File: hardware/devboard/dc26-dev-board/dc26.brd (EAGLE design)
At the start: 126 x 70 mm, 104 parts, among them CN1 JST, IC3 LDL112D33R, J1 DC26 Shitty AddOn, J2 DC26 Shitty AddOn, P1 SSSS811101, Y1 ABL-8.000MHZ-B2

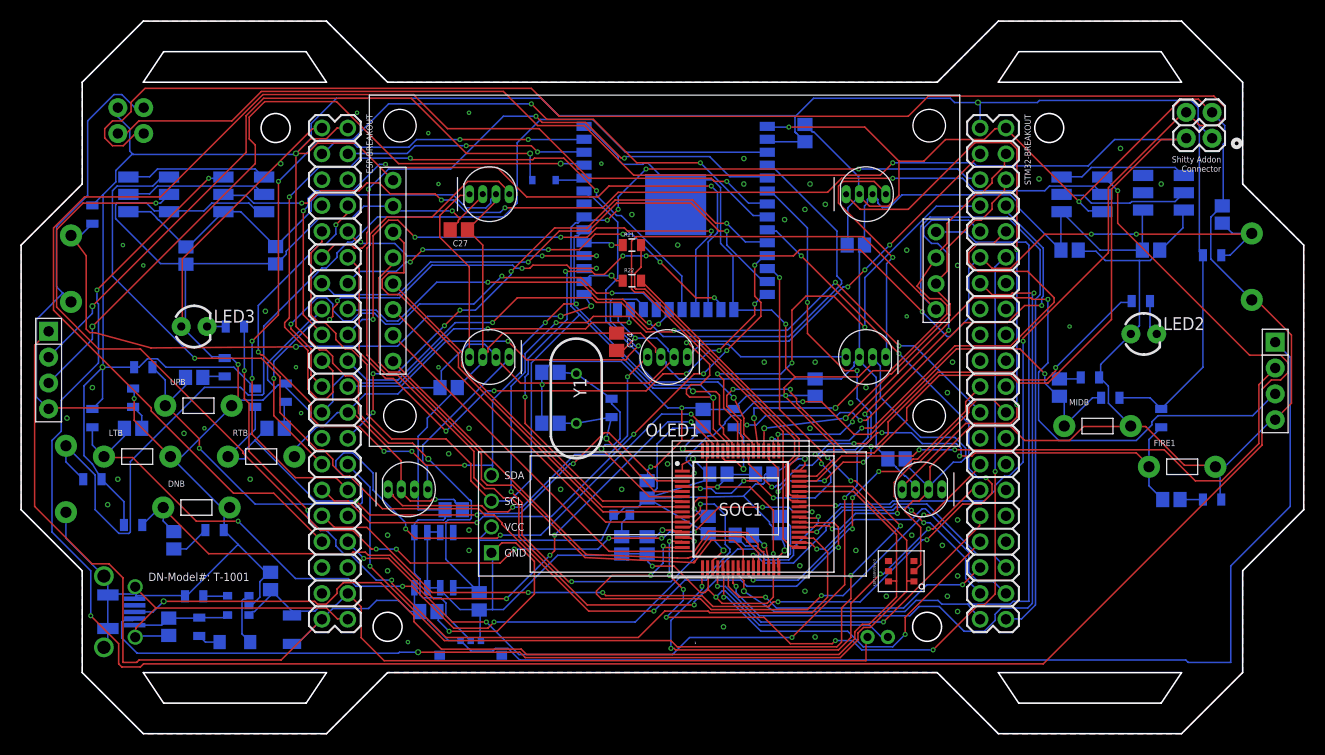
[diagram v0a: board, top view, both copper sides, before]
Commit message: logo causing 0 width polys will fix later
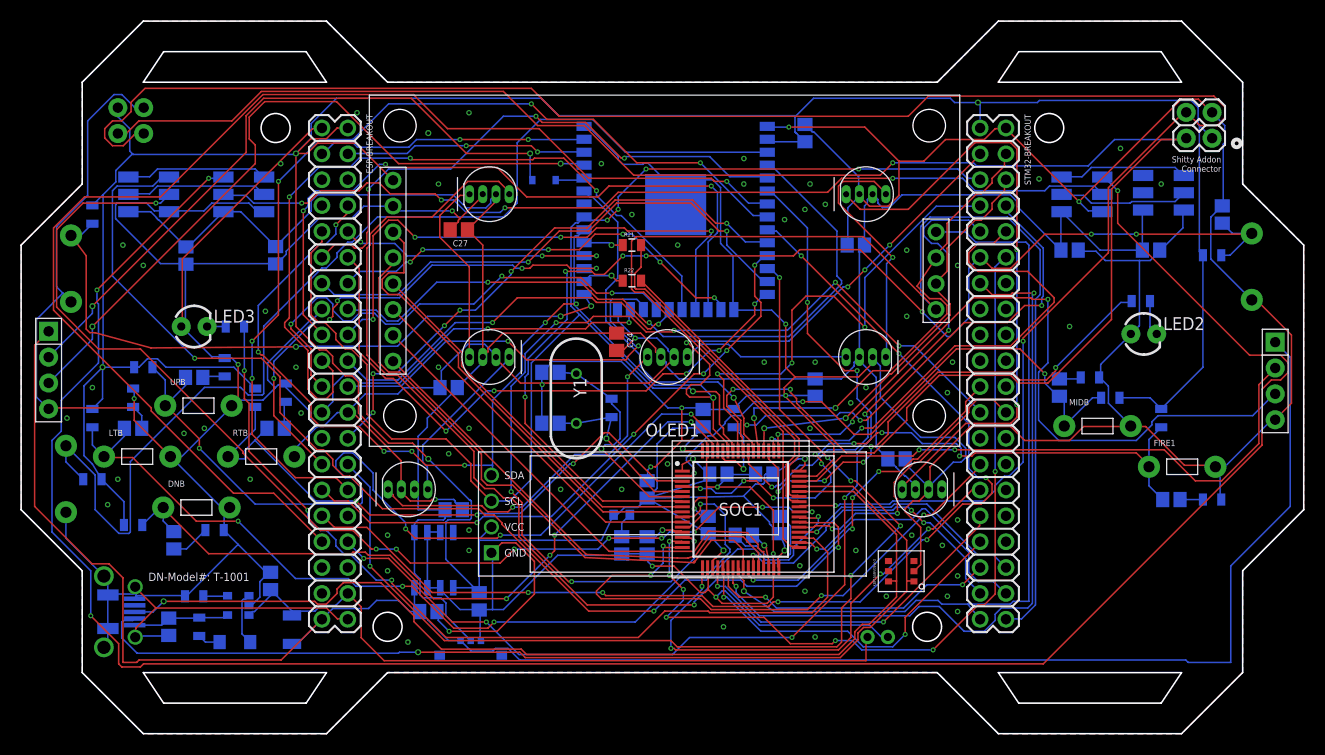
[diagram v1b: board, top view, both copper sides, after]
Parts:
- removed U$1: KRUX_LOGO, dc-26:KRUX_LOGO
- removed U$2: CMD_C0DE_LOGO, dc-26:CMD_C0DE_LOGO
- removed U$3: DARKNET_DD, dc-26:DARKNET_D
- removed U$4: DARKNET_NN, dc-26:DARKNET_N
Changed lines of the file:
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@@
 <setting verticaltext="up"/>
 </settings>
-<grid distance="1" unitdist="mm" unit="mm" style="lines" multiple="1" display="yes" altdistance="0.5" altunitdist="mm" altunit="mm"/>
+<grid distance="39.3700787" unitdist="mil" unit="mil" style="lines" multiple="1" display="yes" altdistance="19.6850394" altunitdist="mil" altunit="mil"/>
 <layers>
 <layer number="1" name="Top" color="4" fill="1" visible="yes" active="yes"/>
@@
 <layer number="27" name="tValues" color="7" fill="1" visible="yes" active="yes"/>
 <layer number="28" name="bValues" color="7" fill="1" visible="yes" active="yes"/>
-<layer number="29" name="tStop" color="7" fill="3" visible="yes" active="yes"/>
+<layer number="29" name="tStop" color="7" fill="3" visible="no" active="yes"/>
 <layer number="30" name="bStop" color="7" fill="6" visible="no" active="yes"/>
 <layer number="31" name="tCream" color="7" fill="4" visible="no" active="yes"/>
@@
 <layer number="119" name="mUnrouted" color="7" fill="1" visible="no" active="yes"/>
 <layer number="120" name="mDimension" color="7" fill="1" visible="no" active="yes"/>
-<layer number="121" name="_tsilk" color="7" fill="1" visible="yes" active="yes"/>
+<layer number="121" name="_tsilk" color="7" fill="1" visible="no" active="yes"/>
 <layer number="122" name="_bsilk" color="7" fill="1" visible="no" active="yes"/>
 <layer number="123" name="tTestmark" color="7" fill="1" visible="no" active="yes"/>
@@
 <circle x="91" y="10.5" radius="1.425" width="0.1524" layer="20"/>
 <circle x="103" y="59.5" radius="1.425" width="0.1524" layer="20"/>
-<text x="104" y="11" size="1.4224" layer="29" font="vector">Darknet
+<text x="104" y="11" size="1.4224" layer="29">Darknet
 Indusries LLC</text>
-<text x="14.5" y="15" size="0.8128" layer="21" font="vector">DN-Model#: T-1001</text>
+<text x="14.5" y="15" size="0.8128" layer="21">DN-Model#: T-1001</text>
 </plain>
 <attributes>
@@
 <attribute name="MANUFACTURER_PART_NUMBER" value="XBP15SRV05W-G" x="88.46" y="15.96" size="1.778" layer="27" rot="R90" display="off"/>
 </element>
-<element name="U$3" library="dc-26" package="DARKNET_D" value="DARKNET_DD" x="45.52" y="59.62"/>
-<element name="U$4" library="dc-26" package="DARKNET_N" value="DARKNET_NN" x="83.44" y="58.62"/>
 <element name="UPB" library="dc-26" package="TACTILE-2PIN-NARROW" value="UserButton" x="19.42" y="32.22"/>
 <element name="USB" library="dc-26" package="DX4R005JJ2" value="DX4R005JJ2DX4R005JJ2" x="13.88" y="11.98" rot="MR0"/>
@@
 <element name="J2" library="dc-26" package="DC26SHITTY_ADDON_CONNECTOR" value="DC26 Shitty AddOn" x="11.5" y="61.5" rot="MR270"/>
 <element name="C4" library="dc-26" package="C0805" value="1uF" x="47" y="13" rot="MR270"/>
-<element name="U$1" library="dc-26" package="KRUX_LOGO" value="KRUX_LOGO" x="71" y="10"/>
-<element name="U$2" library="dc-26" package="CMD_C0DE_LOGO" value="CMD_C0DE_LOGO" x="61" y="10"/>
 </elements>
 <signals>
@@
 <vertex x="8" y="54"/>
 </polygon>
-<via x="20" y="30" extent="1-16" drill="0.2"/>
-<via x="12" y="48" extent="1-16" drill="0.2"/>
-<via x="14" y="46" extent="1-16" drill="0.2"/>
-<via x="29" y="36" extent="1-16" drill="0.2"/>
-<via x="40" y="9" extent="1-16" drill="0.2"/>
-<via x="43" y="54" extent="1-16" drill="0.2"/>
-<via x="105" y="40" extent="1-16" drill="0.2"/>
-<via x="35" y="61" extent="1-16" drill="0.2"/>
-<via x="42" y="59" extent="1-16" drill="0.2"/>
-<via x="46" y="61" extent="1-16" drill="0.2"/>
-<via x="59" y="56" extent="1-16" drill="0.2"/>
-<via x="43" y="36" extent="1-16" drill="0.2"/>
-<via x="29.5" y="31.5" extent="1-16" drill="0.2"/>
-<via x="89" y="41" extent="1-16" drill="0.2"/>
+<via x="20" y="30" extent="1-16" drill="0.3"/>
+<via x="12" y="48" extent="1-16" drill="0.3"/>
+<via x="14" y="46" extent="1-16" drill="0.3"/>
+<via x="29" y="36" extent="1-16" drill="0.3"/>
+<via x="40" y="9" extent="1-16" drill="0.3"/>
+<via x="43" y="54" extent="1-16" drill="0.3"/>
+<via x="105" y="40" extent="1-16" drill="0.3"/>
+<via x="35" y="61" extent="1-16" drill="0.3"/>
+<via x="42" y="59" extent="1-16" drill="0.35"/>
+<via x="46" y="61" extent="1-16" drill="0.3"/>
+<via x="59" y="56" extent="1-16" drill="0.3"/>
+<via x="43" y="36" extent="1-16" drill="0.3"/>
+<via x="29.5" y="31.5" extent="1-16" drill="0.3"/>
+<via x="89" y="41" extent="1-16" drill="0.3"/>
 <via x="61" y="24" extent="1-16" drill="0.3"/>
 <via x="71" y="10.5" extent="1-16" drill="0.3"/>

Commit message: added logo to library added logos to board
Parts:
- added U$1: CMD_C0DE_LOGO, dc-26:CMD_C0DE_LOGO
- added U$2: KRUX_LOGO, dc-26:KRUX_LOGO
- LED1: value MF-LED-0603-GREEN -> MF-LED-1206-GREEN
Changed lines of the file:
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@@
 <setting verticaltext="up"/>
 </settings>
-<grid distance="39.3700787" unitdist="mil" unit="mil" style="lines" multiple="1" display="yes" altdistance="19.6850394" altunitdist="mil" altunit="mil"/>
+<grid distance="0.999999999" unitdist="mm" unit="mm" style="lines" multiple="1" display="yes" altdistance="0.500000001" altunitdist="mm" altunit="mm"/>
 <layers>
 <layer number="1" name="Top" color="4" fill="1" visible="yes" active="yes"/>
@@
 <layer number="27" name="tValues" color="7" fill="1" visible="yes" active="yes"/>
 <layer number="28" name="bValues" color="7" fill="1" visible="yes" active="yes"/>
-<layer number="29" name="tStop" color="7" fill="3" visible="no" active="yes"/>
-<layer number="30" name="bStop" color="7" fill="6" visible="no" active="yes"/>
+<layer number="29" name="tStop" color="7" fill="3" visible="yes" active="yes"/>
+<layer number="30" name="bStop" color="7" fill="6" visible="yes" active="yes"/>
 <layer number="31" name="tCream" color="7" fill="4" visible="no" active="yes"/>
 <layer number="32" name="bCream" color="7" fill="5" visible="no" active="yes"/>
@@
 </element>
 <element name="LCD1" library="dc-26" package="ST7735S_LCD_DISPLAY" value="ST7735S_LCD_MODULE" x="65.21" y="45.48" rot="R270"/>
-<element name="LED1" library="dc-26" package="LED-1206" value="MF-LED-0603-GREEN" x="23" y="9" rot="MR180"/>
+<element name="LED1" library="dc-26" package="LED-1206" value="MF-LED-1206-GREEN" x="23" y="9" rot="MR180"/>
 <element name="LED2" library="dc-26" package="LED3MM" value="LED2-3MM" x="112.29" y="39.27"/>
 <element name="LINK1" library="dc-26" package="1X04" value="STLINK-V2-CONNECTOR" x="125.2" y="33.38" rot="R270"/>
@@
 <element name="J2" library="dc-26" package="DC26SHITTY_ADDON_CONNECTOR" value="DC26 Shitty AddOn" x="11.5" y="61.5" rot="MR270"/>
 <element name="C4" library="dc-26" package="C0805" value="1uF" x="47" y="13" rot="MR270"/>
+<element name="U$1" library="dc-26" package="CMD_C0DE_LOGO" value="CMD_C0DE_LOGO" x="115" y="12" rot="MR0"/>
+<element name="U$2" library="dc-26" package="KRUX_LOGO" value="KRUX_LOGO" x="106" y="12" rot="MR0"/>
 </elements>
 <signals>

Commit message: updated board
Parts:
- RESETTABLE-FUSE: value SSSS811101 -> NANOSMDH075F-02
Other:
- board text added: "DN-Model#: PhC-2000"
- board text added: "Personal Hyperwave Communicator"
- board text removed: "DN-Model#: T-1001"
- board text removed: "Darknet Indusries LLC"
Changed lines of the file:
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@@
 <circle x="91" y="10.5" radius="1.425" width="0.1524" layer="20"/>
 <circle x="103" y="59.5" radius="1.425" width="0.1524" layer="20"/>
-<text x="104" y="11" size="1.4224" layer="29">Darknet
-Indusries LLC</text>
-<text x="14.5" y="15" size="0.8128" layer="21">DN-Model#: T-1001</text>
+<text x="102" y="13" size="1.4224" layer="29">Personal Hyperwave
+Communicator</text>
+<text x="15.5" y="12" size="1.4224" layer="21">DN-Model#:
+   PhC-2000</text>
 </plain>
 <attributes>
@@
 <element name="R8" library="dc-26" package="0805" value="4K7" x="119" y="47" rot="MR180"/>
 <element name="R9" library="dc-26" package="0805" value="1M" x="60" y="32" rot="MR270"/>
-<element name="RESETTABLE-FUSE" library="dc-26" package="PTC-1206" value="SSSS811101" x="28.61" y="10.22" rot="MR270">
-<attribute name="PROD_ID" value="RES-11150" x="28.61" y="10.22" size="1.778" layer="28" rot="MR270" display="off"/>
+<element name="RESETTABLE-FUSE" library="dc-26" package="PTC-1206" value="NANOSMDH075F-02" x="28.61" y="10.22" rot="MR270">
+<attribute name="MANUFACTURE_ID" value="NANOSMDH075F-02" x="28.61" y="10.22" size="1.778" layer="28" rot="MR270" display="off"/>
+<attribute name="PROD_ID" value="NANOSMDH075F-02" x="28.61" y="10.22" size="1.778" layer="28" rot="MR270" display="off"/>
 </element>
 <element name="RTB" library="dc-26" package="TACTILE-2PIN-NARROW" value="UserButton" x="25.58" y="27.22"/>

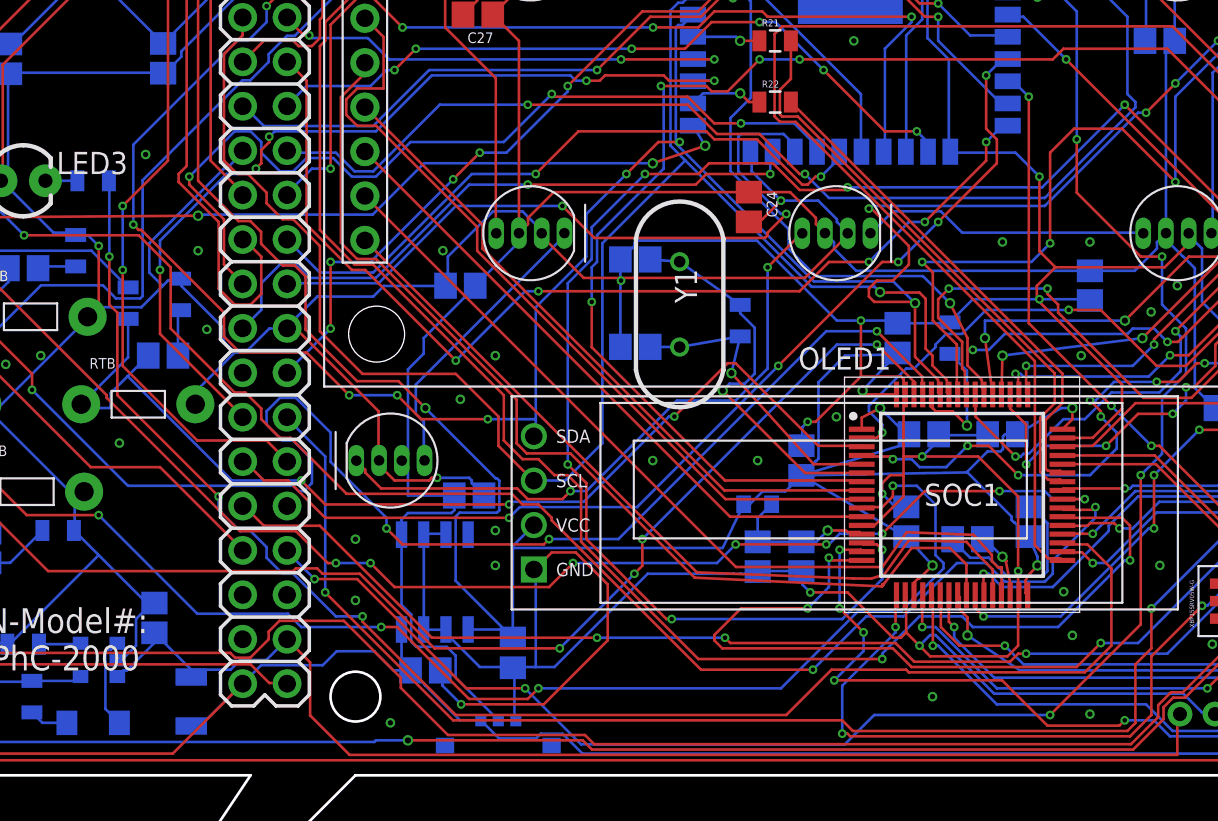
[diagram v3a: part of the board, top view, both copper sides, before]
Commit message: led 3 is now controlled via esp32 rather than STM
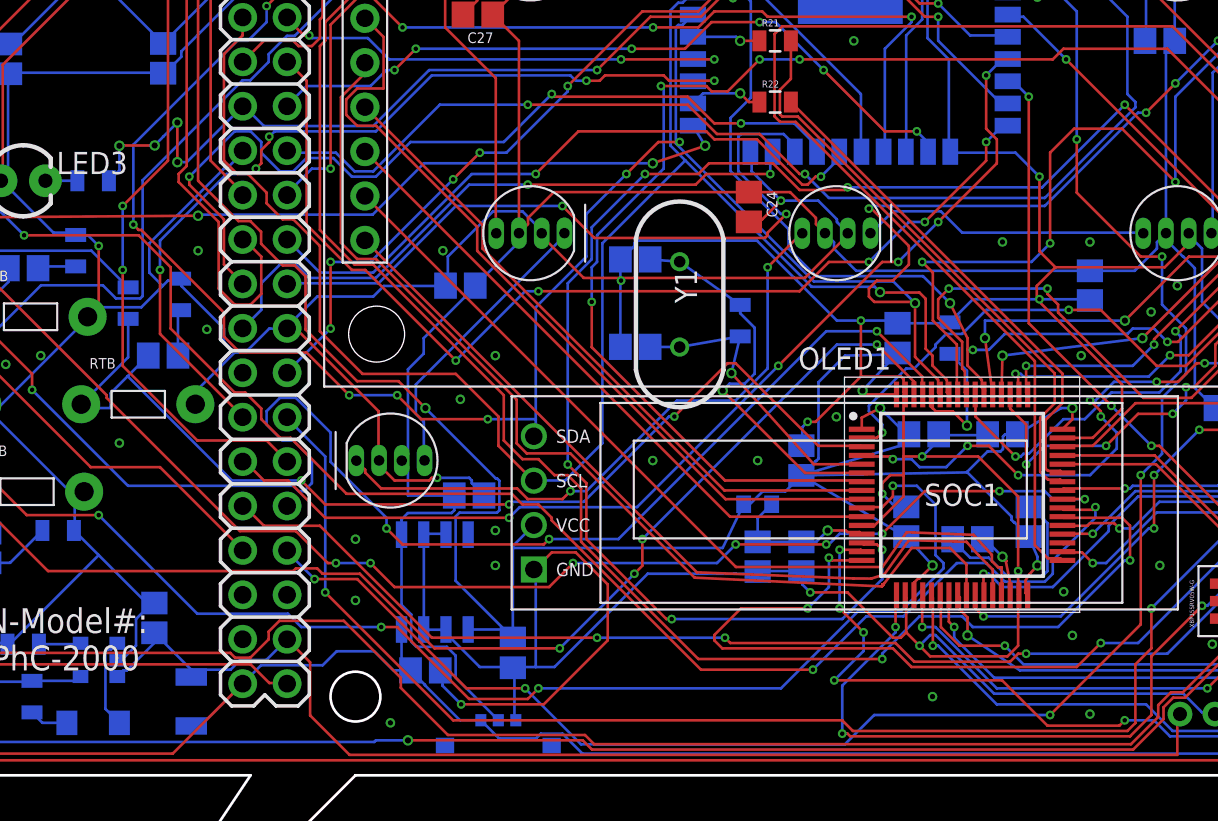
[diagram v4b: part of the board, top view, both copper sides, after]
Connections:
- net IO14: now also R23.1
- net SIMPLE_LED2: no longer R23.1
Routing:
- net SIMPLE_LED2: track 87.5 -> 0.11 mm, vias 3 -> 0
- net IO14: track 52.0 -> 65.5 mm, vias 2 -> 6
- net GND: vias 81 -> 80
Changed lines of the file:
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@@
 <via x="89.5" y="19.5" extent="1-16" drill="0.3"/>
 <via x="87" y="13.5" extent="1-16" drill="0.3"/>
-<via x="26" y="41.5" extent="1-16" drill="0.3"/>
 <via x="27.5" y="56" extent="1-16" drill="0.3"/>
 <via x="6.5" y="31" extent="1-16" drill="0.3"/>
@@
 <via x="71.3232" y="49.3776" extent="1-16" drill="0.254"/>
 <via x="51.816" y="46.3296" extent="1-16" drill="0.254"/>
+<contactref element="R23" pad="1"/>
+<wire x1="23.9268" y1="39.9288" x2="23.9" y2="40" width="0.1524" layer="16"/>
+<via x="26.517178125" y="42.017178125" extent="1-16" drill="0.35"/>
+<wire x1="27.815803125" y1="43.821403125" x2="27.815803125" y2="43.329415625" width="0" layer="19" extent="1-16"/>
+<via x="27.815803125" y="43.329415625" extent="1-16" drill="0.35"/>
+<wire x1="27.815803125" y1="43.329415625" x2="27.815803125" y2="41.062990625" width="0.1524" layer="1"/>
+<wire x1="27.815803125" y1="41.062990625" x2="27.8158" y2="41.0629875" width="0.1524" layer="1"/>
+<via x="27.8158" y="41.0629875" extent="1-16" drill="0.35"/>
+<wire x1="27.8158" y1="41.0629875" x2="28.3529875" y2="41.0629875" width="0.1524" layer="16"/>
+<wire x1="28.3529875" y1="41.0629875" x2="31.55" y2="44.26" width="0.1524" layer="16"/>
+<wire x1="26.517178125" y1="42.017178125" x2="27.017178125" y2="42.530790625" width="0.1524" layer="16"/>
+<wire x1="27.017178125" y1="42.530790625" x2="27.815803125" y2="43.329415625" width="0.1524" layer="16"/>
+<wire x1="23.9" y1="40" x2="24.5" y2="40.6" width="0.1524" layer="16"/>
+<wire x1="24.5" y1="40.6" x2="24.5" y2="42" width="0.1524" layer="16"/>
+<via x="24.5" y="42" extent="1-16" drill="0.35"/>
+<wire x1="24.5" y1="42" x2="24.517178125" y2="42.017178125" width="0.1524" layer="1"/>
+<wire x1="24.517178125" y1="42.017178125" x2="26.517178125" y2="42.017178125" width="0.1524" layer="1"/>
 </signal>
 <signal name="SD2" airwireshidden="yes">
@@
 <signal name="SIMPLE_LED2" airwireshidden="yes">
 <contactref element="SOC1" pad="35"/>
-<contactref element="R23" pad="1"/>
-<wire x1="23.9268" y1="35.6616" x2="23.9268" y2="39.9288" width="0.1524" layer="16"/>
-<wire x1="23.9268" y1="32.9184" x2="23.9268" y2="35.6616" width="0.1524" layer="1"/>
-<wire x1="24.384" y1="32.4612" x2="23.9268" y2="32.9184" width="0.1524" layer="1"/>
-<wire x1="24.384" y1="27.7368" x2="24.384" y2="32.4612" width="0.1524" layer="1"/>
-<wire x1="30.1752" y1="21.9456" x2="24.384" y2="27.7368" width="0.1524" layer="1"/>
-<wire x1="30.1752" y1="21.1836" x2="30.1752" y2="21.9456" width="0.1524" layer="16"/>
-<wire x1="31.3944" y1="19.9644" x2="30.1752" y2="21.1836" width="0.1524" layer="16"/>
-<wire x1="32.004" y1="19.9644" x2="31.3944" y2="19.9644" width="0.1524" layer="16"/>
-<wire x1="32.9184" y1="19.05" x2="32.004" y2="19.9644" width="0.1524" layer="16"/>
-<wire x1="32.9184" y1="18.4404" x2="32.9184" y2="19.05" width="0.1524" layer="16"/>
-<wire x1="33.8328" y1="17.526" x2="32.9184" y2="18.4404" width="0.1524" layer="16"/>
-<wire x1="34.4424" y1="17.526" x2="33.8328" y2="17.526" width="0.1524" layer="16"/>
-<wire x1="36.8808" y1="15.0876" x2="34.4424" y2="17.526" width="0.1524" layer="16"/>
-<wire x1="38.4048" y1="15.0876" x2="36.8808" y2="15.0876" width="0.1524" layer="16"/>
-<wire x1="38.4048" y1="14.7828" x2="38.4048" y2="15.0876" width="0.1524" layer="1"/>
-<wire x1="43.7388" y1="9.4488" x2="38.4048" y2="14.7828" width="0.1524" layer="1"/>
-<wire x1="62.6364" y1="9.4488" x2="43.7388" y2="9.4488" width="0.1524" layer="1"/>
-<wire x1="65.2272" y1="12.0396" x2="62.6364" y2="9.4488" width="0.1524" layer="1"/>
-<wire x1="69.4944" y1="12.0396" x2="65.2272" y2="12.0396" width="0.1524" layer="1"/>
-<wire x1="69.6468" y1="11.8872" x2="69.4944" y2="12.0396" width="0.1524" layer="1"/>
-<wire x1="79.7052" y1="11.8872" x2="69.6468" y2="11.8872" width="0.1524" layer="1"/>
-<wire x1="81.2292" y1="13.4112" x2="79.7052" y2="11.8872" width="0.1524" layer="1"/>
-<wire x1="81.2292" y1="17.8308" x2="81.2292" y2="13.4112" width="0.1524" layer="1"/>
-<wire x1="79.8576" y1="19.2024" x2="81.2292" y2="17.8308" width="0.1524" layer="1"/>
-<wire x1="78.486" y1="19.2024" x2="79.8576" y2="19.2024" width="0.1524" layer="1"/>
-<wire x1="23.9268" y1="39.9288" x2="23.9" y2="40" width="0.1524" layer="16"/>
 <wire x1="78.486" y1="19.2024" x2="78.428" y2="19.29" width="0.1524" layer="1"/>
-<via x="23.9268" y="35.6616" extent="1-16" drill="0.254"/>
-<via x="30.1752" y="21.9456" extent="1-16" drill="0.254"/>
-<via x="38.4048" y="15.0876" extent="1-16" drill="0.254"/>
 </signal>
 <signal name="N$16" airwireshidden="yes">
